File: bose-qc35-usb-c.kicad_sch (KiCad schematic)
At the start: 37 parts, among them J1 502426-2030, J2 2171790001, J3 51281-0598, Q1 BC846BM3T5G, U1 TPS25200

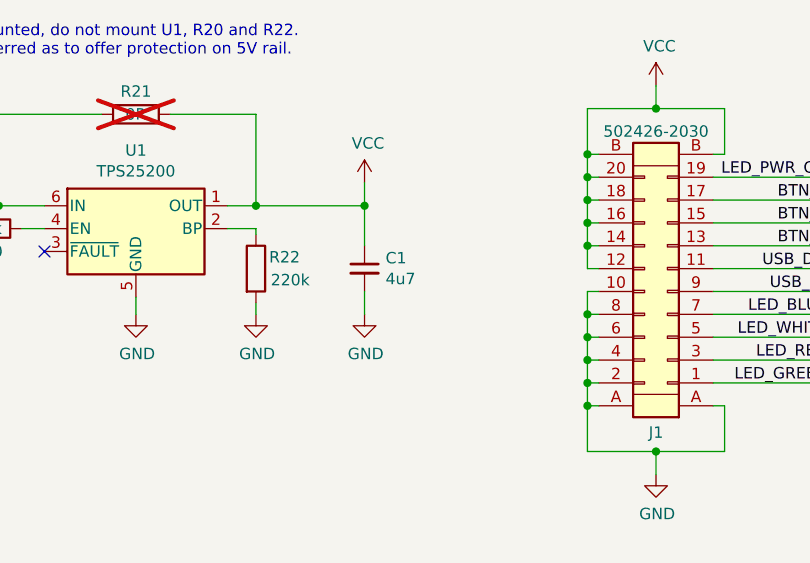
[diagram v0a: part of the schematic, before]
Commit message: increase C1 capacitance
datasheet recommends 20+ µF
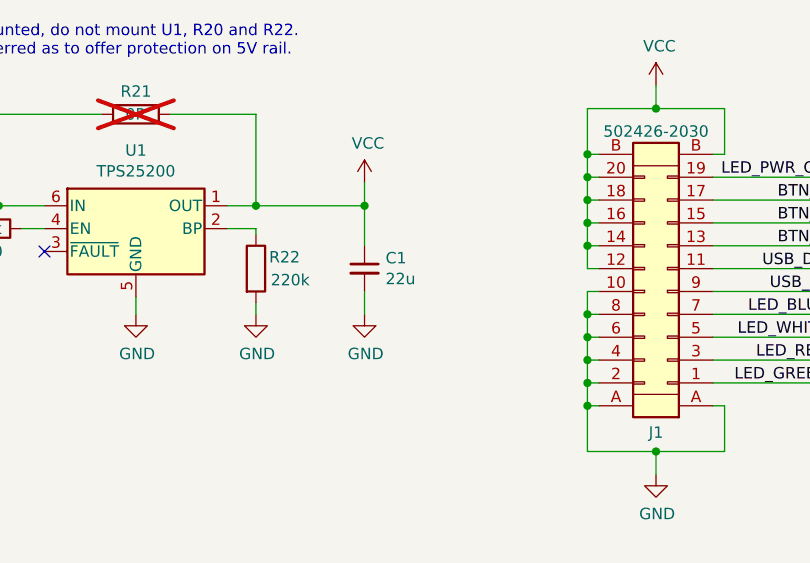
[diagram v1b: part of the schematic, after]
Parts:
- C1: value 4u7 -> 22u
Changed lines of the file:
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@@
       (effects (font (size 1.27 1.27)) (justify left))
     )
-    (property "Value" "4u7" (at 148.3868 50.038 0)
+    (property "Value" "22u" (at 148.3868 50.038 0)
       (effects (font (size 1.27 1.27)) (justify left))
     )
